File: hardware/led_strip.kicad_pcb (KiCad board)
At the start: 2 copper layers, 30 x 30 mm, 42 parts, among them J1 AKL_5_2, J2 AKL_5_2, J3 AKL_5_2, P1 CON-SENSOR, P2 TST, P3 TST, P4 TST, P5 TST, P6 TST, P7 TST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

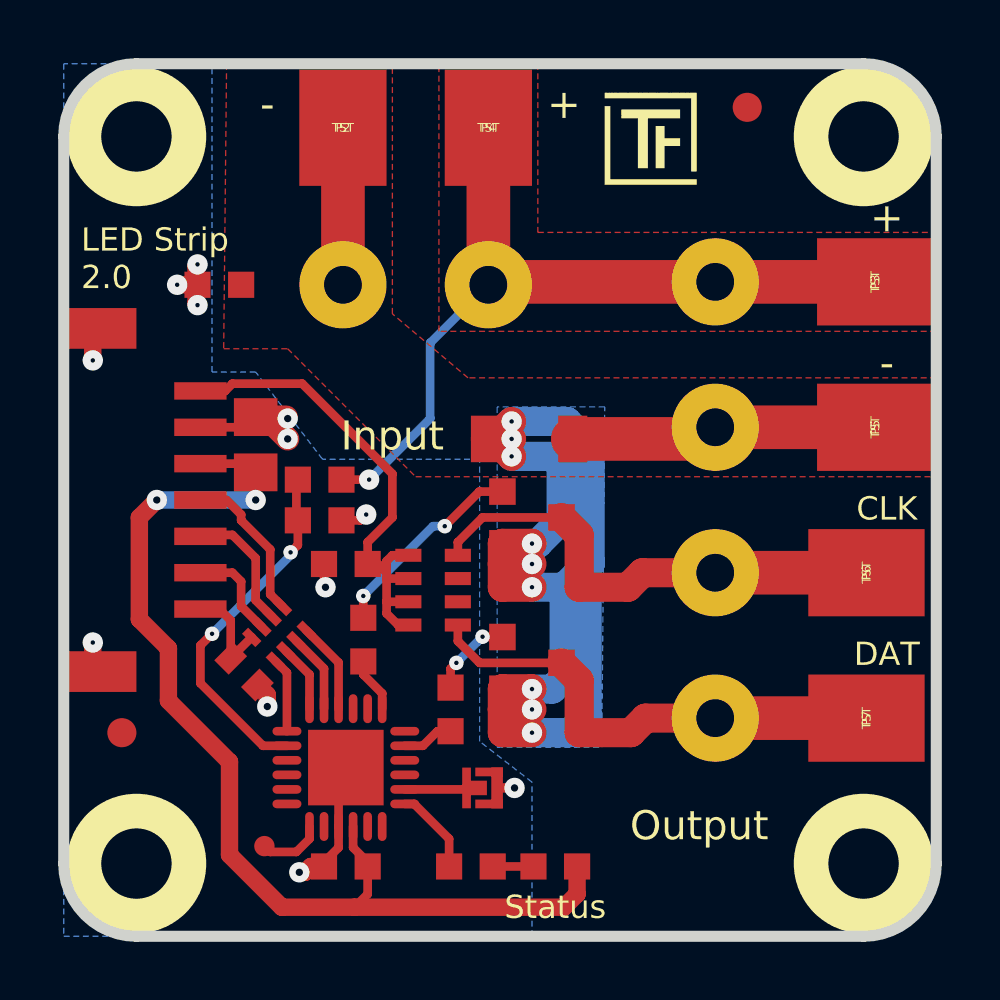
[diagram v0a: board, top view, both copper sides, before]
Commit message: change default via size
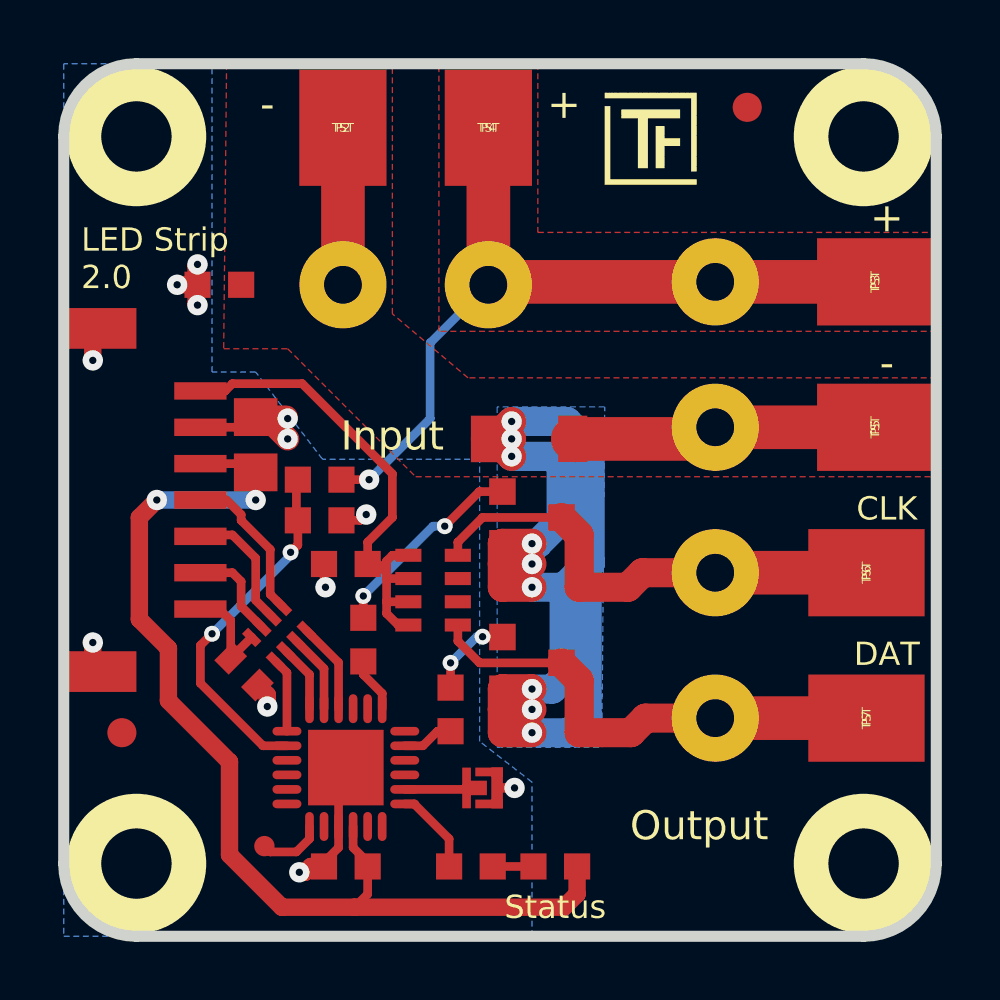
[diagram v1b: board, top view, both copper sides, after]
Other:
- net class Default: via_dia 0.5 -> 0.55; via_drill 0.15 -> 0.25
- rule via_min_drill: 0.15 -> 0.25
- rule via_min_size: 0.5 -> 0.55
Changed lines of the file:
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@@
     (links 66)
     (no_connects 0)
-    (area 42.709499 27.109499 73.090501 57.490501)
+    (area 42.044999 26.444999 282.27147 165.489573)
     (thickness 1.6002)
     (drawings 20)
-    (tracks 248)
+    (tracks 249)
     (zones 0)
     (modules 42)
@@
   )
   (layers
-    (0 Vorderseite signal hide)
+    (0 Vorderseite signal)
     (31 Rückseite signal)
     (32 B.Adhes user)
@@
     (segment_width 0.381)
     (edge_width 0.381)
-    (via_size 0.5)
-    (via_drill 0.15)
-    (via_min_size 0.5)
-    (via_min_drill 0.15)
-    (user_via 0.5 0.15)
+    (via_size 0.55)
+    (via_drill 0.25)
+    (via_min_size 0.55)
+    (via_min_drill 0.25)
+    (user_via 0.55 0.25)
     (user_via 0.7 0.25)
     (uvia_size 0.70104)
@@
     (aux_axis_origin 72.9 27.3)
     (grid_origin 72.9 27.3)
-    (visible_elements FFFFBFBF)
+    (visible_elements FFFFFFBF)
     (pcbplotparams
       (layerselection 0x010fc_80000001)
@@
     (clearance 0.15)
     (trace_width 0.15)
-    (via_dia 0.5)
-    (via_drill 0.15)
+    (via_dia 0.55)
+    (via_drill 0.25)
     (uvia_dia 0.70104)
     (uvia_drill 0.24892)
@@
   (segment (start 49.717401 46.669427) (end 49 45.952026) (width 0.29972) (layer Vorderseite) (net 10))
   (segment (start 57.984 42.011) (end 57.189 42.011) (width 0.29972) (layer Vorderseite) (net 11))
-  (via (at 53.2 45.6) (size 0.5) (drill 0.15) (layers Vorderseite Rückseite) (net 11))
+  (via (at 53.2 45.6) (size 0.55) (drill 0.25) (layers Vorderseite Rückseite) (net 11))
   (segment (start 53.2 45.6) (end 55.6 43.2) (width 0.29972) (layer Rückseite) (net 11))
   (segment (start 55.6 43.2) (end 56 43.2) (width 0.29972) (layer Rückseite) (net 11))
-  (via (at 56 43.2) (size 0.5) (drill 0.15) (layers Vorderseite Rückseite) (net 11))
+  (via (at 56 43.2) (size 0.55) (drill 0.25) (layers Vorderseite Rückseite) (net 11))
   (segment (start 53.2 45.6) (end 53.2 46.35) (width 0.29972) (layer Vorderseite) (net 11))
   (segment (start 57.189 42.011) (end 56 43.2) (width 0.29972) (layer Vorderseite) (net 11))
+  (segment (start 57.3 47) (end 57.1 47) (width 0.29972) (layer Rückseite) (net 12))
+  (segment (start 56.2 47.9) (end 56.2 48.8) (width 0.29972) (layer Vorderseite) (net 12))
+  (via (at 56.2 47.9) (size 0.55) (drill 0.25) (layers Vorderseite Rückseite) (net 12))
+  (segment (start 57.1 47) (end 56.2 47.9) (width 0.29972) (layer Rückseite) (net 12))
+  (segment (start 56.2 48.8) (end 56.2 48.75) (width 0.29972) (layer Vorderseite) (net 12))
   (segment (start 57.984 47.011) (end 57.311 47.011) (width 0.29972) (layer Vorderseite) (net 12))
-  (segment (start 56.2 48.1) (end 56.2 48.75) (width 0.29972) (layer Vorderseite) (net 12))
-  (segment (start 56.4 47.9) (end 56.2 48.1) (width 0.29972) (layer Vorderseite) (net 12))
-  (via (at 56.4 47.9) (size 0.5) (drill 0.15) (layers Vorderseite Rückseite) (net 12))
-  (segment (start 57.3 47) (end 56.4 47.9) (width 0.29972) (layer Rückseite) (net 12))
-  (via (at 57.3 47) (size 0.5) (drill 0.15) (layers Vorderseite Rückseite) (net 12))
+  (via (at 57.3 47) (size 0.55) (drill 0.25) (layers Vorderseite Rückseite) (net 12))
   (segment (start 57.311 47.011) (end 57.3 47) (width 0.29972) (layer Vorderseite) (net 12))
   (segment (start 59 48.8) (end 59.7 48.8) (width 1.00076) (layer Rückseite) (net 13))
@@
   (segment (start 50.95 43.85) (end 50.95 43) (width 0.29972) (layer Vorderseite) (net 15))
   (segment (start 50.7 44.1) (end 50.95 43.85) (width 0.29972) (layer Vorderseite) (net 15))
-  (via (at 50.7 44.1) (size 0.5) (drill 0.15) (layers Vorderseite Rückseite) (net 15))
+  (via (at 50.7 44.1) (size 0.55) (drill 0.25) (layers Vorderseite Rückseite) (net 15))
   (segment (start 50.7 44.2) (end 50.7 44.1) (width 0.29972) (layer Rückseite) (net 15))
   (segment (start 48 46.9) (end 50.7 44.2) (width 0.29972) (layer Rückseite) (net 15))
-  (via (at 48 46.9) (size 0.5) (drill 0.15) (layers Vorderseite Rückseite) (net 15))
+  (via (at 48 46.9) (size 0.55) (drill 0.25) (layers Vorderseite Rückseite) (net 15))
   (segment (start 47.6 47.3) (end 48 46.9) (width 0.29972) (layer Vorderseite) (net 15))
   (segment (start 47.6 48.6) (end 47.6 47.3) (width 0.29972) (layer Vorderseite) (net 15))

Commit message: specify processor
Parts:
- U1: value XMC1XXX24 -> XMC1302
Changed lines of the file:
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@@
   )
   (setup
-    (last_trace_width 0.29972)
+    (last_trace_width 0.15)
     (user_trace_width 0.29972)
     (user_trace_width 0.59944)
@@
       (effects (font (size 0.3 0.3) (thickness 0.075)))
     )
-    (fp_text value XMC1XXX24 (at 0 0.8) (layer F.Fab)
+    (fp_text value XMC1302 (at 0 0.8) (layer F.Fab)
       (effects (font (size 0.3 0.3) (thickness 0.075)))
     )

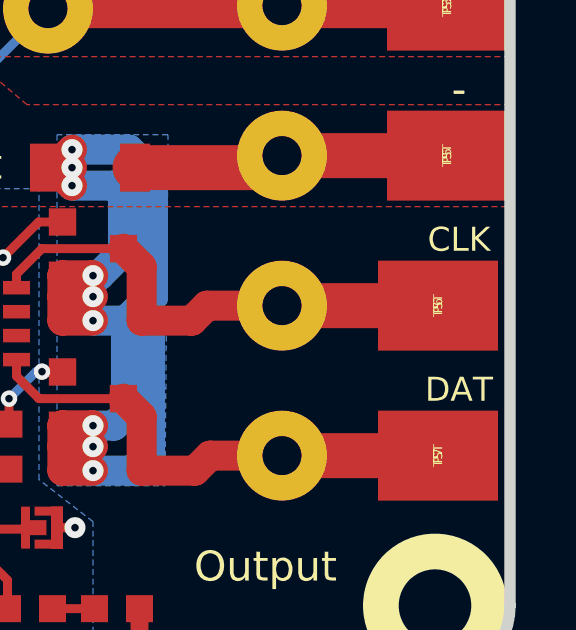
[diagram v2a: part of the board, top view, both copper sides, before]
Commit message: fix description text
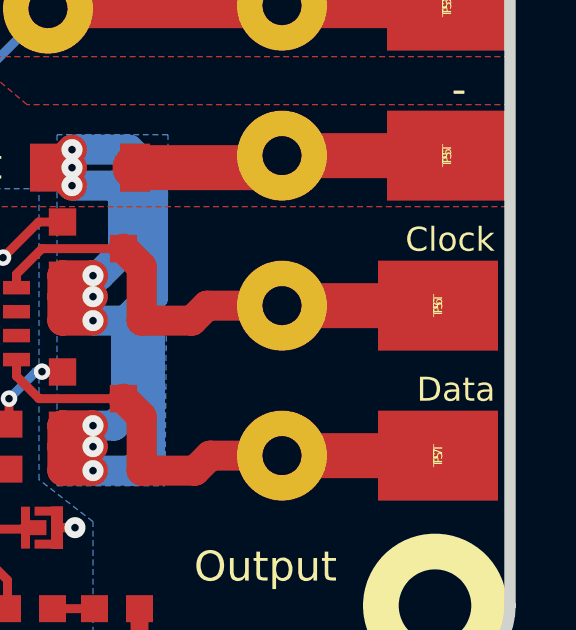
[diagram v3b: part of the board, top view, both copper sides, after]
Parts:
- turned VAL to 0 degrees
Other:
- board text added: "Clock"
- board text added: "Data"
- board text removed: "CLK"
- board text removed: "DAT"
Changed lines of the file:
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@@
   )
   (layers
-    (0 Vorderseite signal)
-    (31 Rückseite signal)
+    (0 Vorderseite signal hide)
+    (31 Rückseite signal hide)
     (32 B.Adhes user)
     (33 F.Adhes user)
@@
     (aux_axis_origin 72.9 27.3)
     (grid_origin 72.9 27.3)
-    (visible_elements FFFFFFBF)
+    (visible_elements FFFFBFBF)
     (pcbplotparams
       (layerselection 0x010fc_80000001)
@@
   )
   (module kicad-libraries:CE_5mm (layer Rückseite)
-    (at 57.9 39.3 180)
-    (fp_text reference VAL (at 0 0 180) (layer B.SilkS) hide
+    (at 57.9 39.3)
+    (fp_text reference VAL (at 0 0) (layer B.SilkS) hide
       (effects (font (size 0.2 0.2) (thickness 0.05)) (justify mirror))
     )
-    (fp_text value CE_5mm (at 0 0 180) (layer B.SilkS) hide
+    (fp_text value CE_5mm (at 0 0) (layer B.SilkS) hide
       (effects (font (size 0.2 0.2) (thickness 0.05)) (justify mirror))
     )
@@
     (effects (font (size 1 1) (thickness 0.15)))
   )
-  (gr_text DAT (at 71.2 47.6) (layer F.SilkS)
+  (gr_text Data (at 71.1 47.6) (layer F.SilkS)
     (effects (font (size 0.8 0.8) (thickness 0.15)))
   )
@@
     (effects (font (size 1 1) (thickness 0.15)))
   )
-  (gr_text CLK (at 71.2 42.6) (layer F.SilkS)
+  (gr_text Clock (at 70.9 42.6) (layer F.SilkS)
     (effects (font (size 0.8 0.8) (thickness 0.15)))
   )
